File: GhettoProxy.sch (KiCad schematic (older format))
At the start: 22 parts, among them IC1 ATMEGA328P-A, P1 OpenLRS, P2 Telemetrie, U1 MIC5205 3,3v, Y1 RESONATEUR

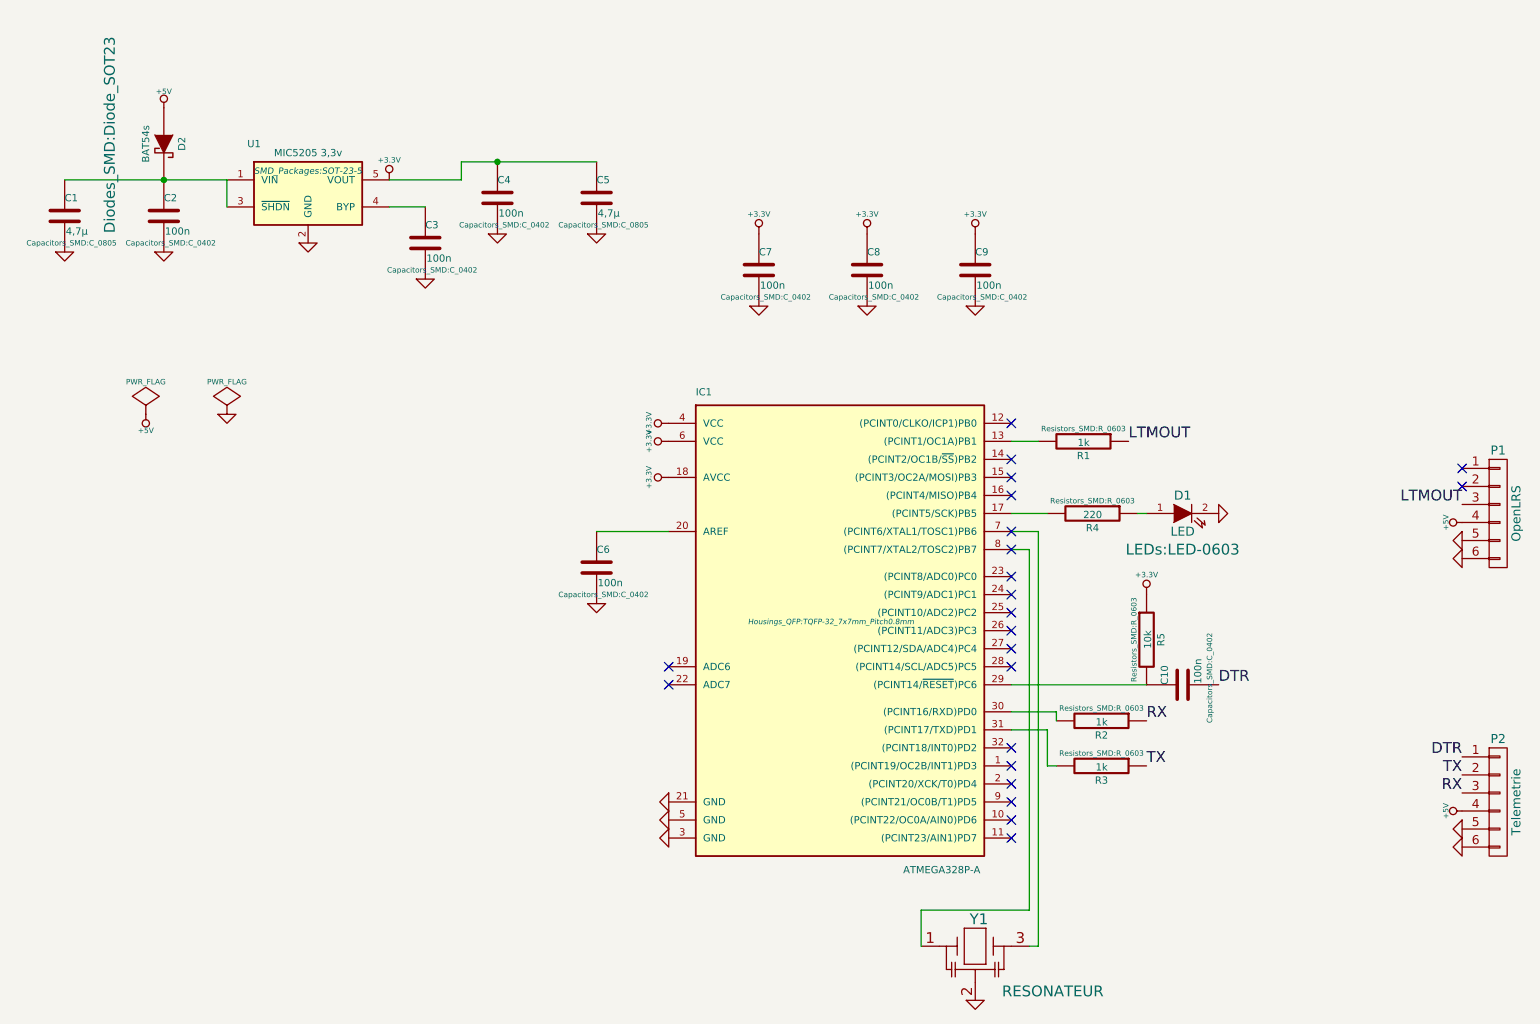
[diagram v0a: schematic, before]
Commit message: 3,3V LDO entfernt (macht keinen Sinn und kostet nur Geld), Platine verkleinert
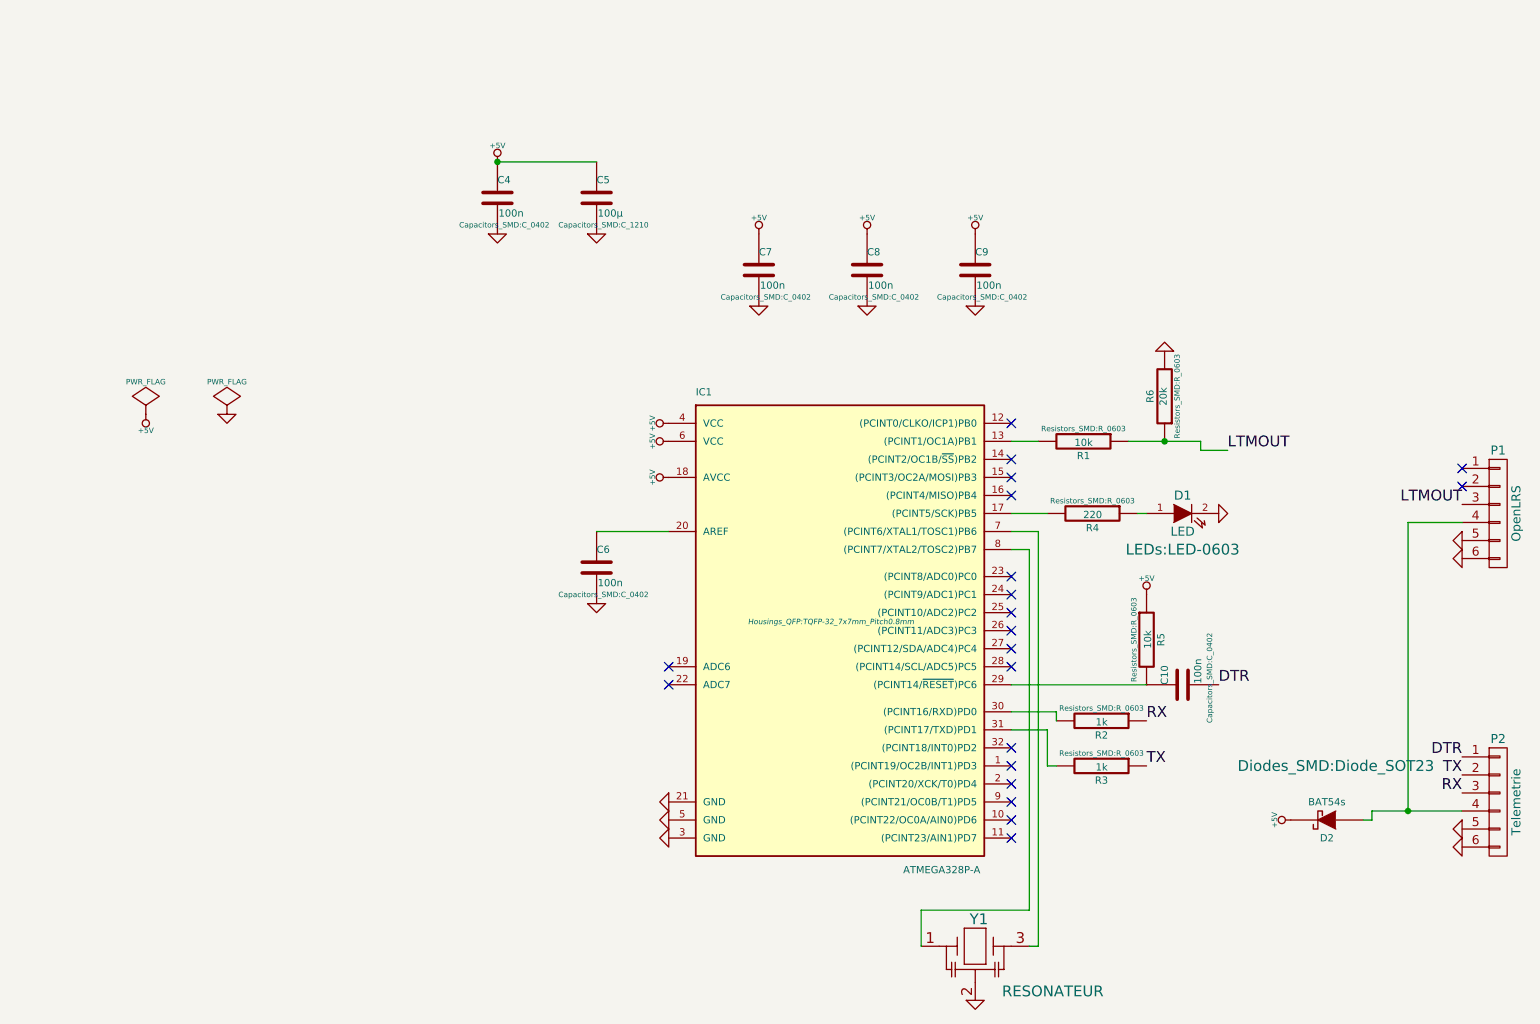
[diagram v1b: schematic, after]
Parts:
- removed C1: 4,7µ, Capacitors_SMD:C_0805, symbol C
- removed C2, C3: 100n, Capacitors_SMD:C_0402, symbol C
- removed U1: MIC5205 3,3v, SMD_Packages:SOT-23-5, symbol APE8865Y5-33-HF-3
- added R6: 20k, Resistors_SMD:R_0603, symbol R
- C5: value 4,7µ -> 100µ; footprint Capacitors_SMD:C_0805 -> Capacitors_SMD:C_1210
- R1: value 1k -> 10k
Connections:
- net +3.3V is gone; now on net +5V: C4.1, C5.1, C7.1, C8.1, C9.1, IC1.18 (AVCC), IC1.4 (VCC), IC1.6 (VCC), R5.1
- net +5V: now also D2.2 (K); no longer D2.1 (A), P1.4 (P4), P2.4 (P4)
- net GND: now also R6.2
- net LTMOUT: now also R6.1
- new net: D2.1 (A), P1.4 (P4), P2.4 (P4)
- no-connect marks 22 -> 20
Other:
- moved on the sheet: D2
